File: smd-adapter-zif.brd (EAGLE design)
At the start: 36.8 x 34.3 mm, 2 parts

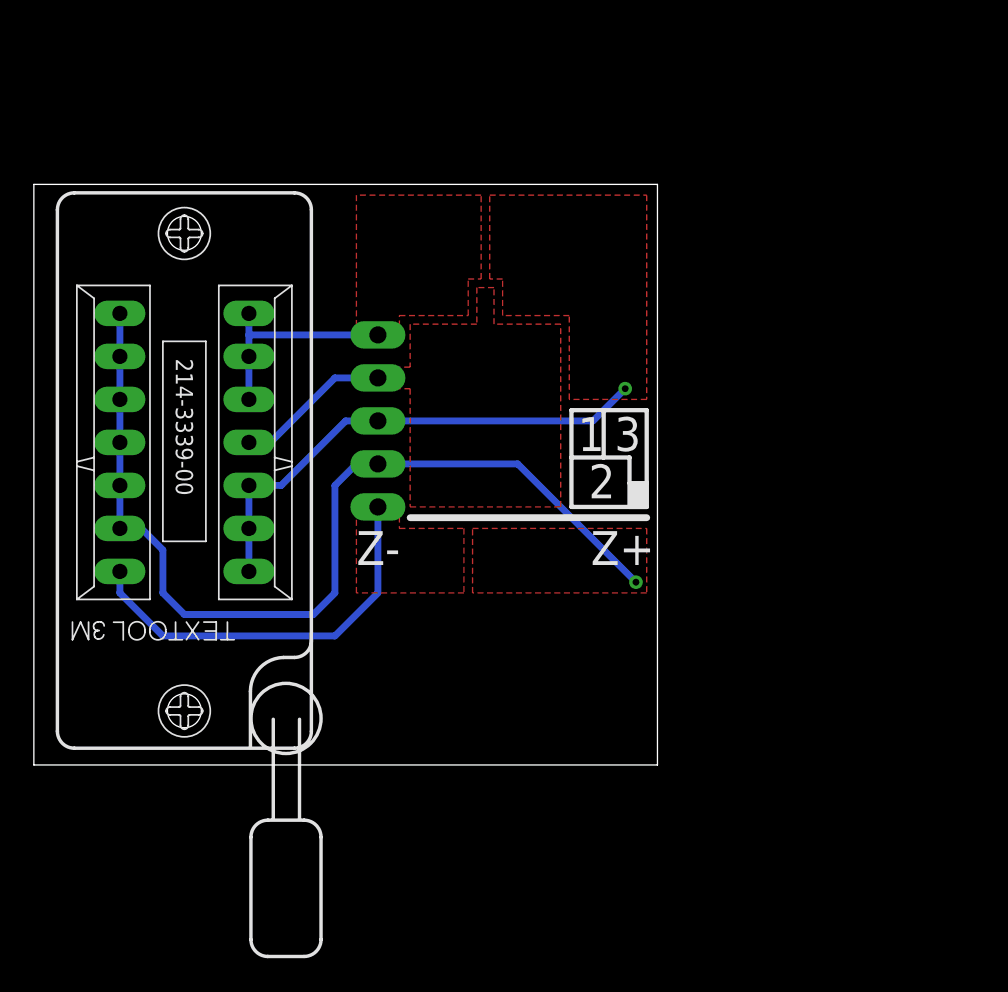
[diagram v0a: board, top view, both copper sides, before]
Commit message: add silk screen for zif pin usage
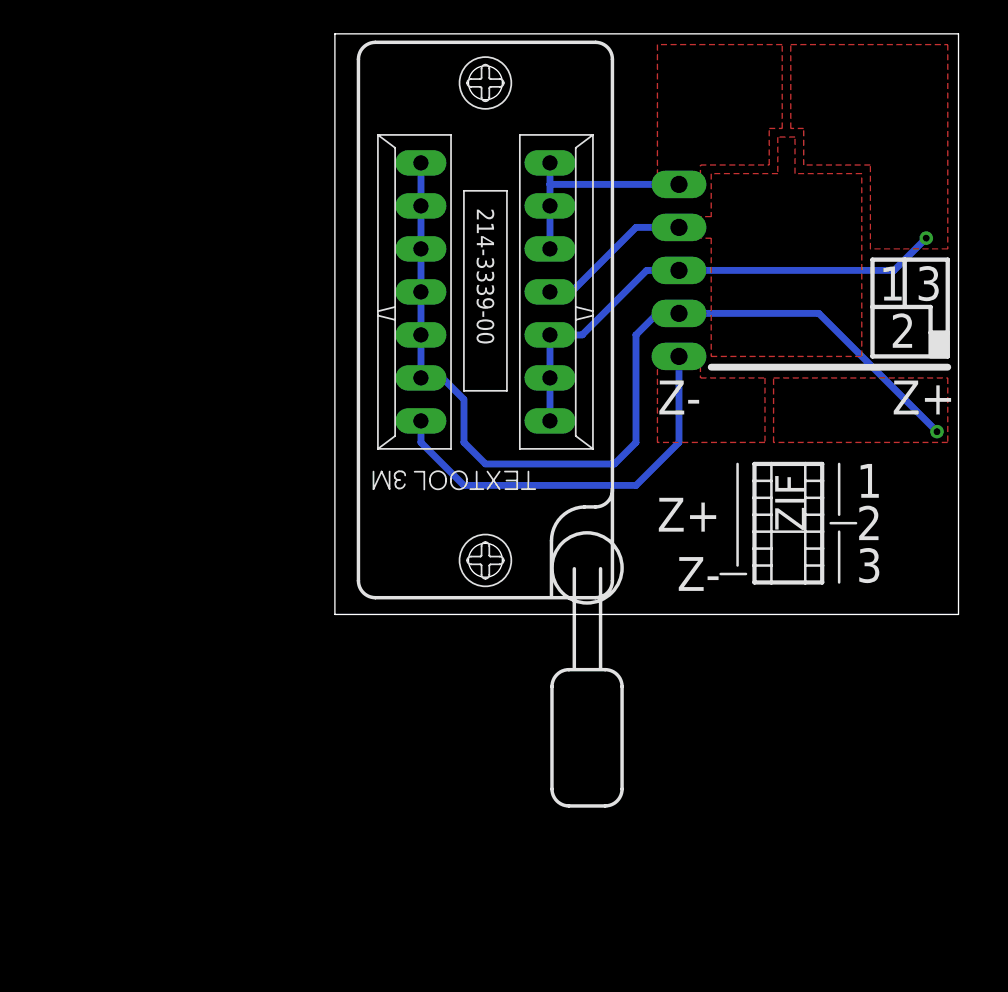
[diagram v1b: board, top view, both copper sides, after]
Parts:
- moved E$1 19.9 mm to (8.89, 19.1)
- moved JP5 19.9 mm to (20.3, 20.3)
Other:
- board text added: "ZIF"
